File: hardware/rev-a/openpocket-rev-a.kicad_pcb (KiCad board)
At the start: 8 copper layers, 115 x 72 mm, 315 parts, among them J1 ER-TFT050A3-2 FFC, J11 5.8 GHz antenna U.FL, J12 push-push microSD, J13 speaker solder pads, J14 SSD1306 128x64 OLED pads, J15 expander developer pads, J18 rotary encoder control pads, J19 ARM switch pads, J2 USB-C, J20 AUX2 three-position switch pa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, J21 AUX3 three-position switch pa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, J22 AUX4 three-position switch pa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, J23 AIL trim pads, J24 ELE trim pads, J25 THR trim pads, J26 RUD trim pads, J3 battery/NTC, J4 speaker connector, J5 master switch, J6 ELRS, J7 left gimbal, J8 right gimbal, J9 menu/UI control pads, Q1 dual protection FET, Q2 Q_BUZZ buzzer MOSFET, U1 ESP32-S3-MINI-1U-N8, U10 display 3V3 buck, U11 analog OSD, U12 OSD 3V3-to-5V, U13 OSD 5V-to-3V3, U14 CVBS TFT controller, U15 AMT boot flash, U16 AMT flash mux, U17 backlight boost, U18 GPIO expander 0x20, U19 GPIO expander 0x21, U2 1S charger/power path, U20 master load switch, U21 I2S speaker amplifier, U22 3V3_SD load switch, U3 1S protector, U4 fuel gauge, U5 3V3 buck-boost, U6 5V boost, U7 5V_VIDEO load switch, U8 5V_DISPLAY load switch, U9 5V_ELRS load switch, Y1 27.000MHz, Y2 27.000MHz

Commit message: fix(rev-a): clear TFT FFC breakout corridor
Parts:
- C22: moved to B.Cu
- moved U20 33.2 mm to (62.0, 62.0)
- moved D1 27.6 mm to (58.0, 56.0)
- moved C54 20.8 mm to (52.0, 55.0), turned to 180 degrees
- moved U17 19.1 mm to (53.0, 60.0)
- moved C55 15.2 mm to (48.0, 55.0), turned to 180 degrees
- moved R87 14.2 mm to (51.0, 52.0), turned to 180 degrees
- moved C56 14.0 mm to (48.0, 53.0), turned to 180 degrees
- moved R88 13.0 mm to (52.0, 53.0), turned to 180 degrees
- moved U10 12.0 mm to (72.0, 54.0)
- moved R86 9.65 mm to (46.5, 51.5), turned to 180 degrees
- moved U4 8.25 mm to (12.0, 53.0)
- moved C22 7.21 mm to (13.0, 55.0), turned to 180 degrees
- moved R25 7.21 mm to (16.0, 52.0)
- moved R26 7.21 mm to (18.0, 52.0)
- moved R27 7.21 mm to (20.0, 52.0)
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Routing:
- net GND: track 272.4 -> 272.9 mm, vias 145 -> 146

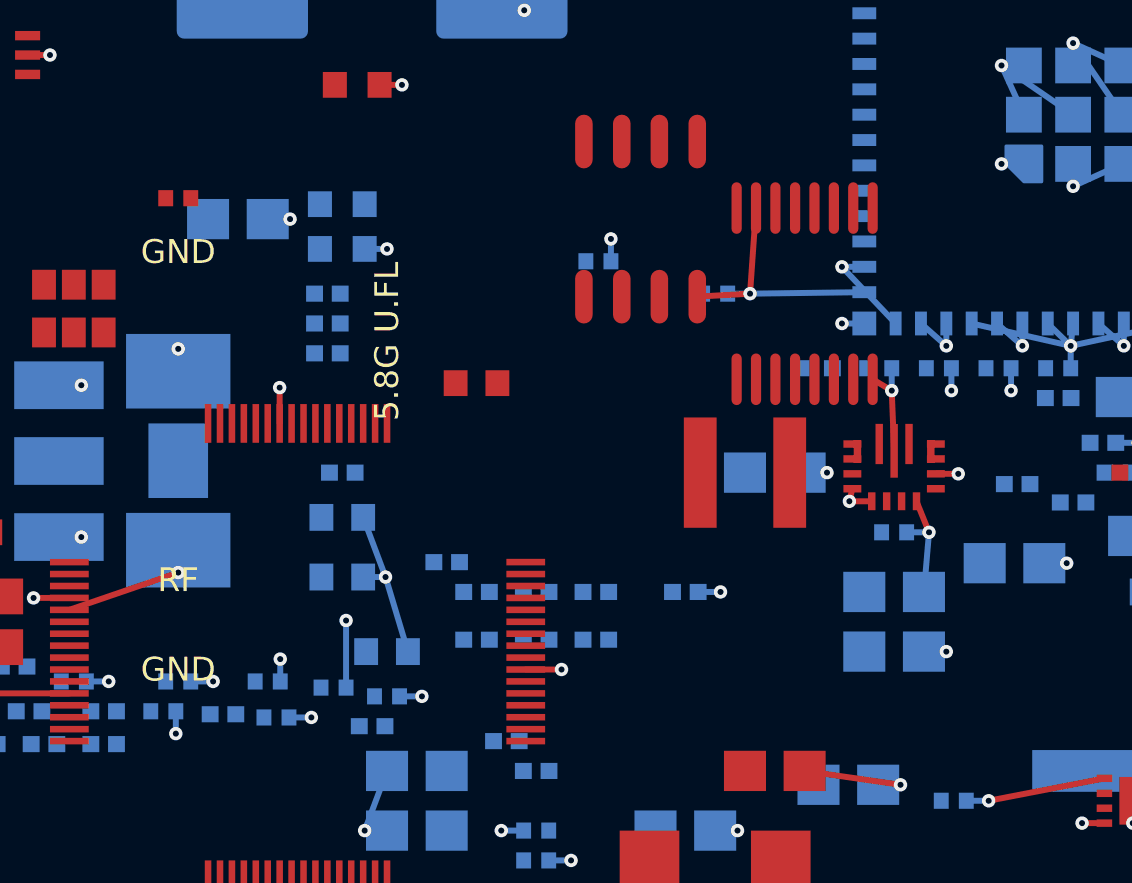
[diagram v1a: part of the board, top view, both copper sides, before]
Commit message: fix(rev-a): clear AMT fanout and refresh placement assets
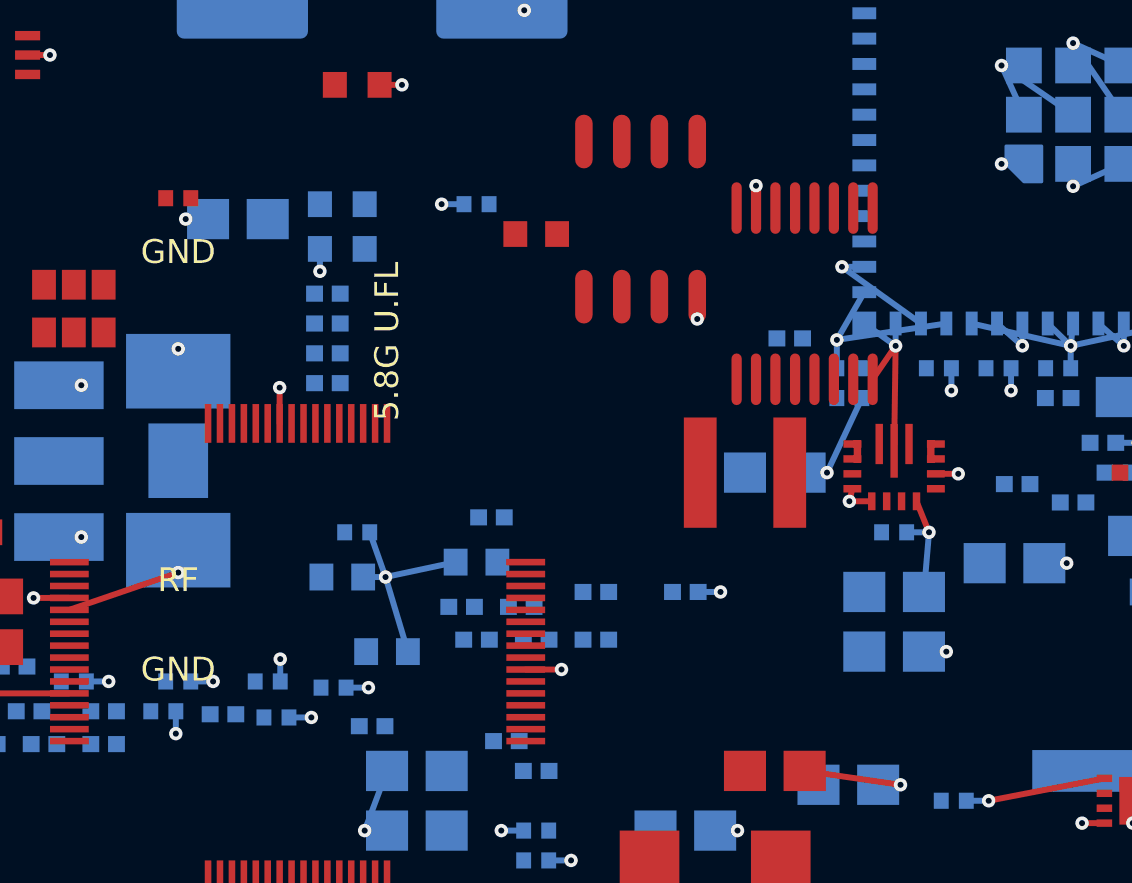
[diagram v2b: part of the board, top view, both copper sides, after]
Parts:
- moved C73 5.59 mm to (46.0, 45.0)
- moved FB3 5.39 mm to (52.0, 35.0)
- moved C71 5.15 mm to (62.5, 39.5), turned to 180 degrees
- moved C11 4.74 mm to (50.0, 46.0), turned to 180 degrees
- moved C70 4.51 mm to (50.0, 34.0), turned to 180 degrees
- moved R77 3.04 mm to (45.0, 40.0), turned to 180 degrees
- moved R89 2.12 mm to (50.5, 44.5)
- moved C78 1.41 mm to (62.5, 40.5)
- moved R95 1.41 mm to (60.5, 38.5)
- moved R13 0.71 mm to (49.5, 47.5)
- moved R90 0.71 mm to (51.5, 47.5)
- turned C60 to 180 degrees
- turned R11 to 180 degrees
- turned R12 to 180 degrees
- turned R53 to 180 degrees
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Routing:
- net GND: track 272.9 -> 275.4 mm, vias 146 -> 145

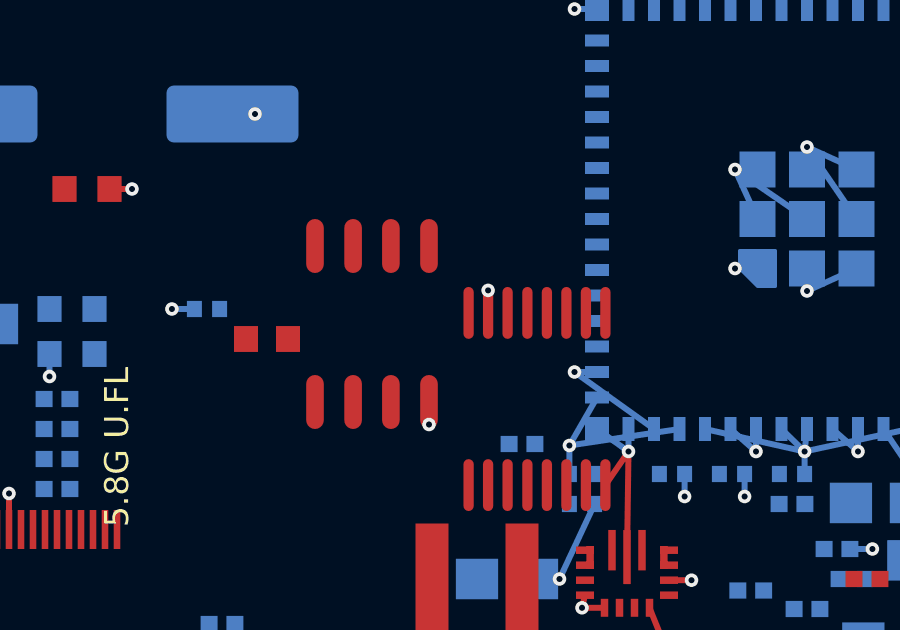
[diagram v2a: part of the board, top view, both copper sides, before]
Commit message: fix(rev-a): seed legal AMT flash fanout
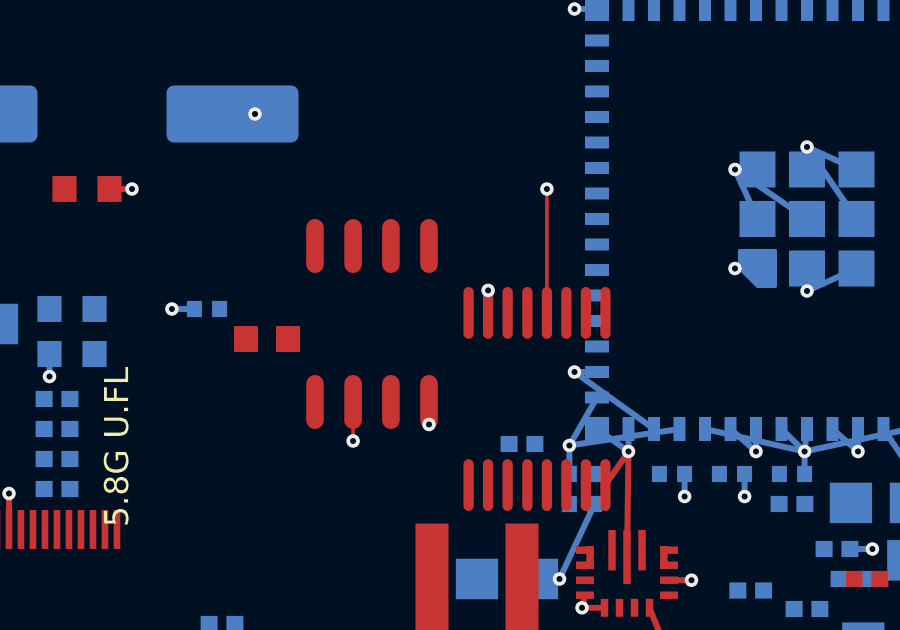
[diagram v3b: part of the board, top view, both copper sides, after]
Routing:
- net AMT_FLASH_C_MISO: track 0.00 -> 24.3 mm, vias 0 -> 2
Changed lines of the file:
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@@
+	)
+	(segment
+		(start 54.87 37.1)
+		(end 54.87 38.4)
+		(width 0.12)
+		(layer "F.Cu")
+		(net 33)
+	)
+	(segment
+		(start 61.33 30)
+		(end 61.33 34.13)
+		(width 0.12)
+		(layer "F.Cu")
+		(net 33)
+	)
+	(via
+		(at 61.33 30)
+		(size 0.45)
+		(drill 0.2)
+		(layers "F.Cu" "B.Cu")
+		(net 33)
+	)
+	(via
+		(at 54.87 38.4)
+		(size 0.45)
+		(drill 0.2)
+		(layers "F.Cu" "B.Cu")
+		(net 33)
+	)
+	(segment
+		(start 54.87 38.4)
+		(end 54.87 28)
+		(width 0.12)
+		(layer "In3.Cu")
+		(net 33)
+	)
+	(segment
+		(start 61.33 28)
+		(end 61.33 30)
+		(width 0.12)
+		(layer "In3.Cu")
+		(net 33)
+	)
+	(segment
+		(start 54.87 28)
+		(end 61.33 28)
+		(width 0.12)
+		(layer "In3.Cu")
+		(net 33)
 	)
 	(segment

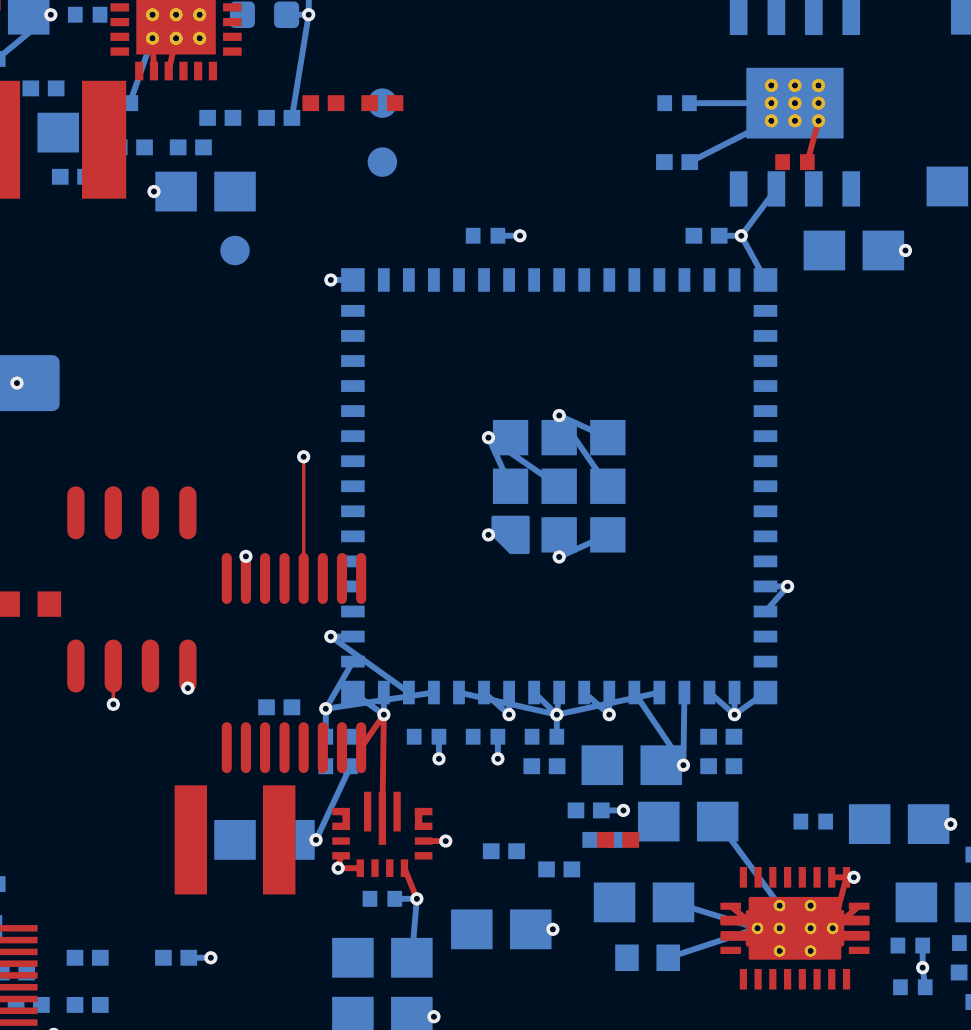
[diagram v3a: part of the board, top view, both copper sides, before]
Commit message: fix(rev-a): center ESP fanout corridor
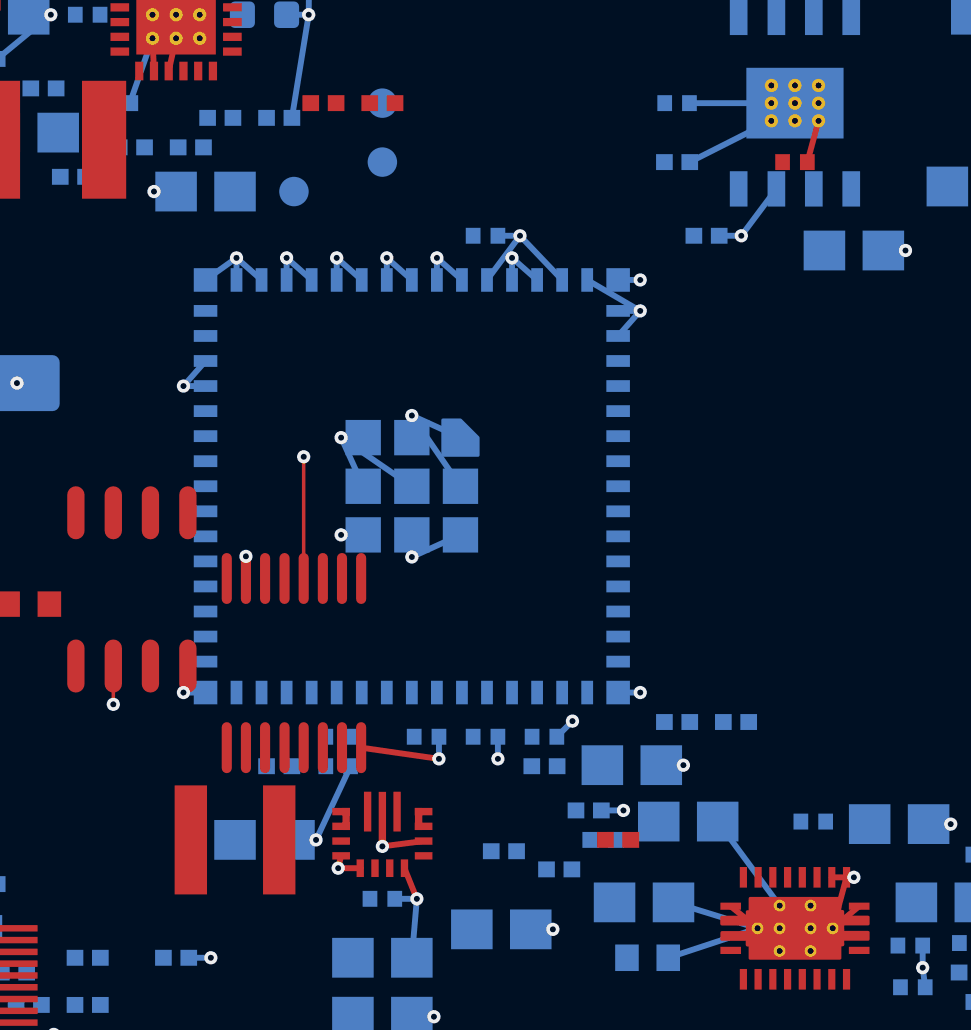
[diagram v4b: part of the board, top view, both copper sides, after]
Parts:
- moved U1 5.00 mm to (65.0, 31.0), turned to 180 degrees
- moved TP44 2.83 mm to (61.0, 21.0)
- moved R95 2.00 mm to (60.5, 40.5)
- moved R97 1.58 mm to (74.0, 39.0)
- moved R98 1.58 mm to (76.0, 39.0)
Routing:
- net GND: track 275.4 -> 261.5 mm, vias 145 -> 147
- net AMT_FLASH_C_MISO: track 24.3 -> 29.3 mm

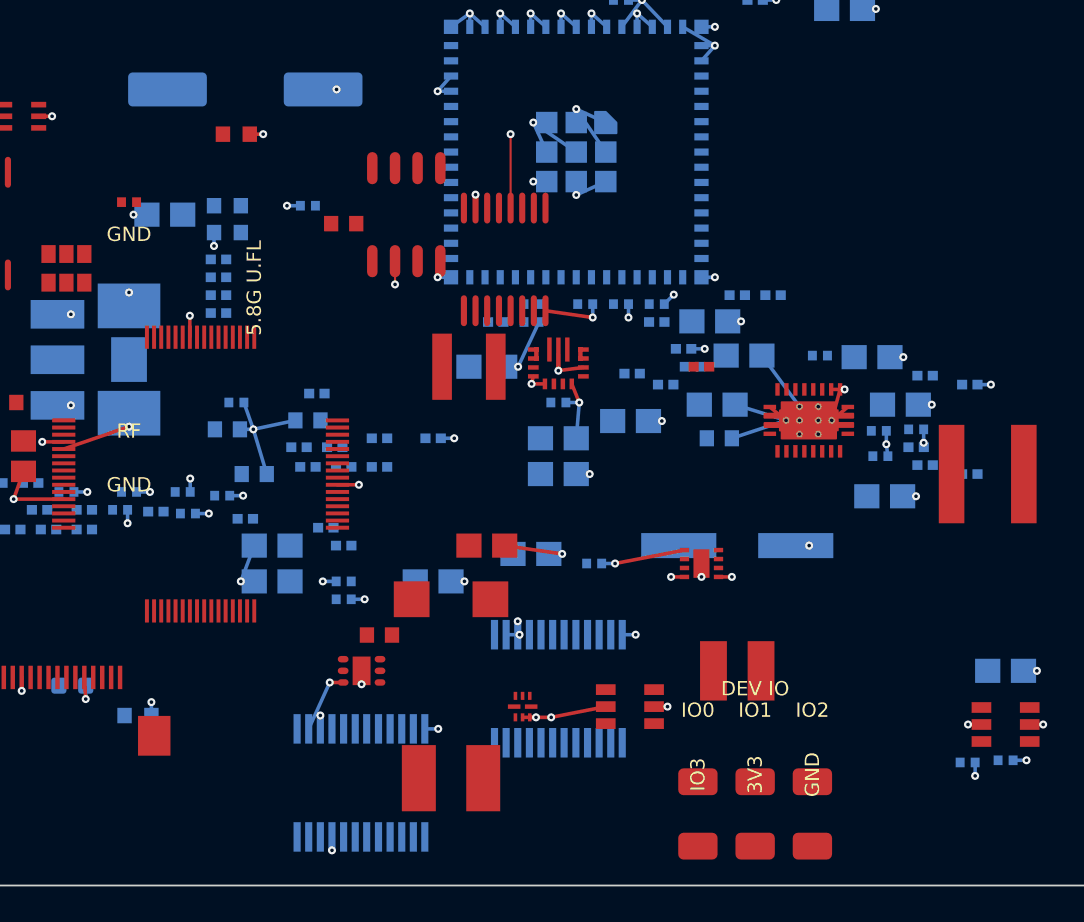
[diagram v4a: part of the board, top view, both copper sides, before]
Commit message: fix(rev-a): tighten ESP and expander routing corridor
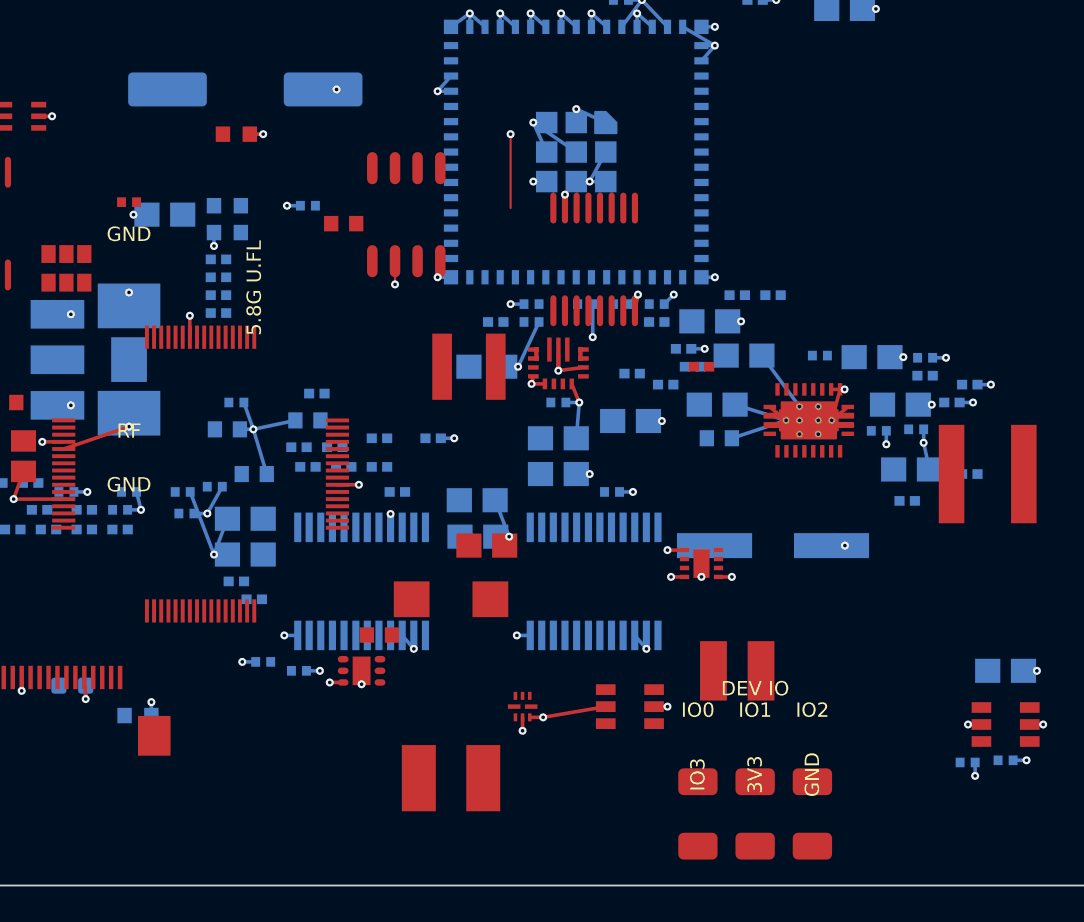
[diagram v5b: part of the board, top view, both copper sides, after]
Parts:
- moved U18 11.3 mm to (53.0, 55.0), turned to 180 degrees
- moved C54 6.36 mm to (47.5, 59.5)
- moved U19 6.32 mm to (66.0, 55.0), turned to 180 degrees
- moved C44 6.04 mm to (84.5, 42.5)
- moved R87 5.66 mm to (47.0, 56.0)
- moved U16 5.00 mm to (66.0, 37.0)
- moved C64 4.72 mm to (49.5, 60.0)
- moved C51 4.24 mm to (59.5, 50.5)
- moved R88 4.24 mm to (55.0, 50.0)
- moved C65 4.12 mm to (67.0, 50.0)
- moved C19 3.54 mm to (59.5, 52.5)
- moved R86 3.54 mm to (46.0, 55.0)
- moved R24 3.20 mm to (86.0, 45.0)
- moved C72 2.24 mm to (43.2, 51.2)
- moved R51 2.24 mm to (83.5, 50.5)
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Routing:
- net GND: track 261.5 -> 259.4 mm, vias 147 -> 145
